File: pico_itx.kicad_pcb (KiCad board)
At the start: 2 copper layers, 100 x 72 mm, 4 parts

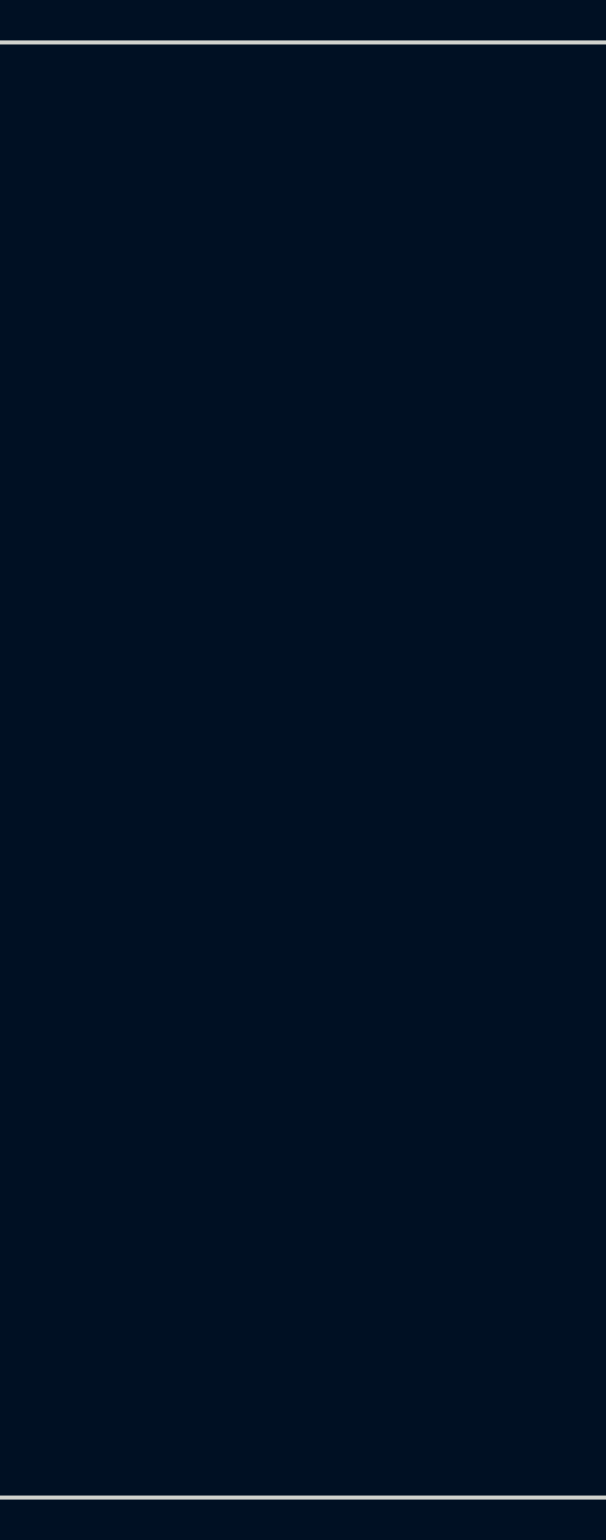
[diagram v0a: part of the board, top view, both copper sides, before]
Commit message: update for pico-itx-template,
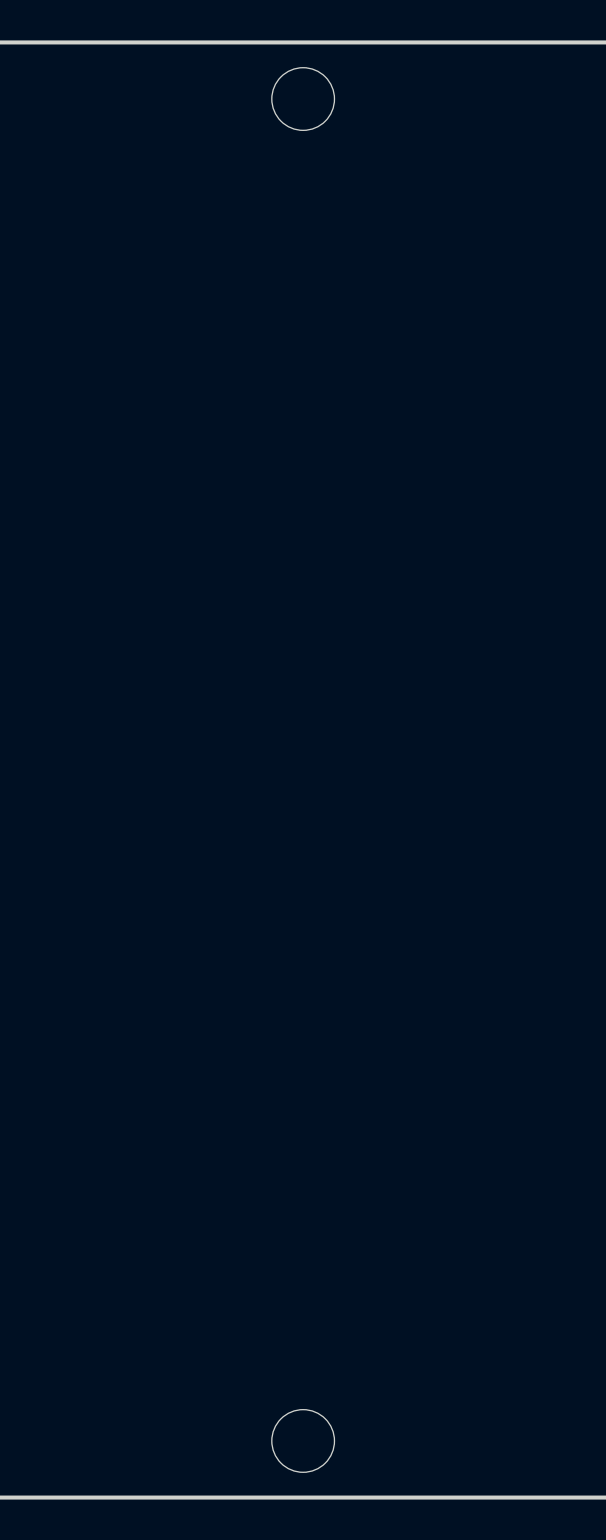
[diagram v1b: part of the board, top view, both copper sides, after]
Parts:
- added H4: MOUNT_M3, footprint-lib:MountingHole_3.1mm_M3,rpi_like, F.Cu at (50.3, 39.3)
- added H4: MOUNT_M3, footprint-lib:MountingHole_3.1mm_M3,rpi_like, F.Cu at (50.3, 105.7)
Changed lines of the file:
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@@
     (tracks 0)
     (zones 0)
-    (modules 4)
+    (modules 6)
     (nets 1)
   )
@@
     (uvia_drill 0.1)
   )
+  (module footprint-lib:MountingHole_3.1mm_M3,rpi_like (layer F.Cu)
+    (at 50.3 39.3)
+    (descr "Mounting Hole 2.7mm, no annular, M2.5")
+    (tags "mounting hole 2.7mm no annular m2.5")
+    (attr virtual)
+    (fp_text reference H4 (at 0 -3.7) (layer F.SilkS) hide
+      (effects (font (size 1 1) (thickness 0.15)))
+    )
+    (fp_text value MOUNT_M3 (at 0 3.7) (layer F.Fab)
+      (effects (font (size 1 1) (thickness 0.15)))
+    )
+    (fp_circle (center 0 0) (end 2.7 0) (layer Cmts.User) (width 0.15))
+    (fp_circle (center 0 0) (end 2.95 0) (layer F.CrtYd) (width 0.05))
+    (fp_circle (center 0 0) (end 1.905 0) (layer F.Mask) (width 1.2))
+    (fp_circle (center 0 0) (end 1.905 0) (layer B.Mask) (width 1.2))
+    (fp_text user %R (at 0.3 0) (layer F.Fab)
+      (effects (font (size 1 1) (thickness 0.15)))
+    )
+    (pad "" np_thru_hole circle (at 0 0) (size 3.1 3.1) (drill 3.1) (layers *.Cu *.Mask)
+      (solder_mask_margin 1.5) (clearance 1.5))
+  )
+  (module footprint-lib:MountingHole_3.1mm_M3,rpi_like (layer F.Cu)
+    (at 50.3 105.7)
+    (descr "Mounting Hole 2.7mm, no annular, M2.5")
+    (tags "mounting hole 2.7mm no annular m2.5")
+    (attr virtual)
+    (fp_text reference H4 (at 0 -3.7) (layer F.SilkS) hide
+      (effects (font (size 1 1) (thickness 0.15)))
+    )
+    (fp_text value MOUNT_M3 (at 0 3.7) (layer F.Fab)
+      (effects (font (size 1 1) (thickness 0.15)))
+    )
+    (fp_text user %R (at 0.3 0) (layer F.Fab)
+      (effects (font (size 1 1) (thickness 0.15)))
+    )
+    (fp_circle (center 0 0) (end 1.905 0) (layer B.Mask) (width 1.2))
+    (fp_circle (center 0 0) (end 1.905 0) (layer F.Mask) (width 1.2))
+    (fp_circle (center 0 0) (end 2.95 0) (layer F.CrtYd) (width 0.05))
+    (fp_circle (center 0 0) (end 2.7 0) (layer Cmts.User) (width 0.15))
+    (pad "" np_thru_hole circle (at 0 0) (size 3.1 3.1) (drill 3.1) (layers *.Cu *.Mask)
+      (solder_mask_margin 1.5) (clearance 1.5))
+  )
   (module footprint-lib:MountingHole_3.1mm_M3,rpi_like locked (layer F.Cu)
